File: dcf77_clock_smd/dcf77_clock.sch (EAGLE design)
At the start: 24 parts, among them IC1 7805DT, IC2 ATMEGA48/88/168-AU, J2 DCJ0202, U1 LCD-16X2SILK

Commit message: Update capacitors footprints
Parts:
- removed EN1: PEC11, bourns:PEC11
- added C3: (no value), rcl:CPOL-EUSMCZ
- added SW1: EC12E_SW, switch-alps:EC12E_SW
- C2: device rcl:CPOL-EUE2-5 -> rcl:CPOL-EUUD-4X5,8
- LED1: device SparkFun:LED-FKIT-1206 -> led:LEDCHIP-LED0805
- Q1: device crystal:CRYSTALSM49 -> crystal:CRYSTALMM39SL
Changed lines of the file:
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@@
 <part name="U$1" library="SparkFun" deviceset="AVR_SPI_PROG2" device="PTH2"/>
 <part name="U1" library="SparkFun" deviceset="LCD-16X2" device="SILK"/>
-<part name="LED1" library="SparkFun" deviceset="LED" device="-FKIT-1206"/>
+<part name="LED1" library="led" library_urn="urn:adsk.eagle:library:259" deviceset="LED" device="CHIP-LED0805" package3d_urn="urn:adsk.eagle:package:15818/2"/>
 <part name="IC2" library="atmega8" deviceset="ATMEGA48/88/168" device="-AU"/>
 <part name="U$4" library="SparkFun" deviceset="DS1307" device="SO8"/>
 <part name="IC1" library="linear" library_urn="urn:adsk.eagle:library:262" deviceset="78*" device="DT" package3d_urn="urn:adsk.eagle:package:16415/2" technology="05" value="7805DT"/>
 <part name="J2" library="con-jack" library_urn="urn:adsk.eagle:library:154" deviceset="DCJ0202" device="" package3d_urn="urn:adsk.eagle:package:7491/1"/>
-<part name="Q1" library="crystal" library_urn="urn:adsk.eagle:library:204" deviceset="CRYSTAL" device="SM49" package3d_urn="urn:adsk.eagle:package:12085/1"/>
+<part name="Q1" library="crystal" library_urn="urn:adsk.eagle:library:204" deviceset="CRYSTAL" device="MM39SL" package3d_urn="urn:adsk.eagle:package:12090/1"/>
 <part name="R1" library="SparkFun" deviceset="TRIMPOT" device="PTH"/>
 <part name="H1" library="holes" library_urn="urn:adsk.eagle:library:237" deviceset="MOUNT-HOLE" device="3.2" package3d_urn="urn:adsk.eagle:package:14275/1" value="MOUNT-HOLE3.2"/>
@@
 <part name="GND1" library="supply1" library_urn="urn:adsk.eagle:library:371" deviceset="GND" device=""/>
 <part name="C1" library="rcl" library_urn="urn:adsk.eagle:library:334" deviceset="C-EU" device="C0805K" package3d_urn="urn:adsk.eagle:package:23681/2" value="100n"/>
-<part name="EN1" library="bourns" deviceset="PEC11" device=""/>
 <part name="L1" library="rcl" library_urn="urn:adsk.eagle:library:334" deviceset="L-EU" device="L1812" package3d_urn="urn:adsk.eagle:package:23494/2"/>
-<part name="C2" library="rcl" library_urn="urn:adsk.eagle:library:334" deviceset="CPOL-EU" device="E2-5" package3d_urn="urn:adsk.eagle:package:23346/2"/>
+<part name="C2" library="rcl" library_urn="urn:adsk.eagle:library:334" deviceset="CPOL-EU" device="UD-4X5,8" package3d_urn="urn:adsk.eagle:package:23474/1"/>
 <part name="MOD1" library="dcf77" deviceset="DCF77MODULE" device=""/>
 <part name="HOLD1" library="dcf77" deviceset="COREHOLDER" device=""/>
@@
 <part name="H3" library="holes" library_urn="urn:adsk.eagle:library:237" deviceset="MOUNT-HOLE" device="3.2" package3d_urn="urn:adsk.eagle:package:14275/1" value="MOUNT-HOLE3.2"/>
 <part name="H4" library="holes" library_urn="urn:adsk.eagle:library:237" deviceset="MOUNT-HOLE" device="3.2" package3d_urn="urn:adsk.eagle:package:14275/1" value="MOUNT-HOLE3.2"/>
+<part name="SW1" library="switch-alps" library_urn="urn:adsk.eagle:library:373" deviceset="EC12E_SW" device="" package3d_urn="urn:adsk.eagle:package:27083/1"/>
+<part name="C3" library="rcl" library_urn="urn:adsk.eagle:library:334" deviceset="CPOL-EU" device="SMCZ" package3d_urn="urn:adsk.eagle:package:25927/3"/>
 </parts>
 <sheets>
@@
 <attribute name="VALUE" x="-9.144" y="13.081" size="1.778" layer="96" rot="MR0"/>
 </instance>
-<instance part="EN1" gate="1" x="99.06" y="30.48" smashed="yes">
-<attribute name="NAME" x="95.25" y="35.56" size="1.778" layer="95"/>
-<attribute name="VALUE" x="93.98" y="24.13" size="1.778" layer="96"/>
-</instance>
 <instance part="L1" gate="G$1" x="-45.72" y="86.36" smashed="yes">
 <attribute name="NAME" x="-54.8386" y="143.51" size="1.778" layer="95" rot="R90"/>
@@
 <attribute name="VALUE" x="144.272" y="-35.4838" size="1.778" layer="96"/>
 </instance>
+<instance part="SW1" gate="G$1" x="129.54" y="106.68" smashed="yes">
+<attribute name="PART" x="125.73" y="106.68" size="1.27" layer="95" rot="R90"/>
+<attribute name="VALUE" x="135.89" y="106.68" size="1.27" layer="96" rot="R90"/>
+</instance>
+<instance part="SW1" gate="G$2" x="149.86" y="114.3" smashed="yes">
+<attribute name="PART" x="144.78" y="119.38" size="1.27" layer="95"/>
+<attribute name="VALUE" x="144.78" y="111.76" size="1.27" layer="96"/>
+</instance>
+<instance part="C3" gate="G$1" x="-127" y="83.82" smashed="yes">
+<attribute name="NAME" x="-125.857" y="84.3026" size="1.778" layer="95"/>
+<attribute name="VALUE" x="-125.857" y="79.2226" size="1.778" layer="96"/>
+</instance>
 </instances>

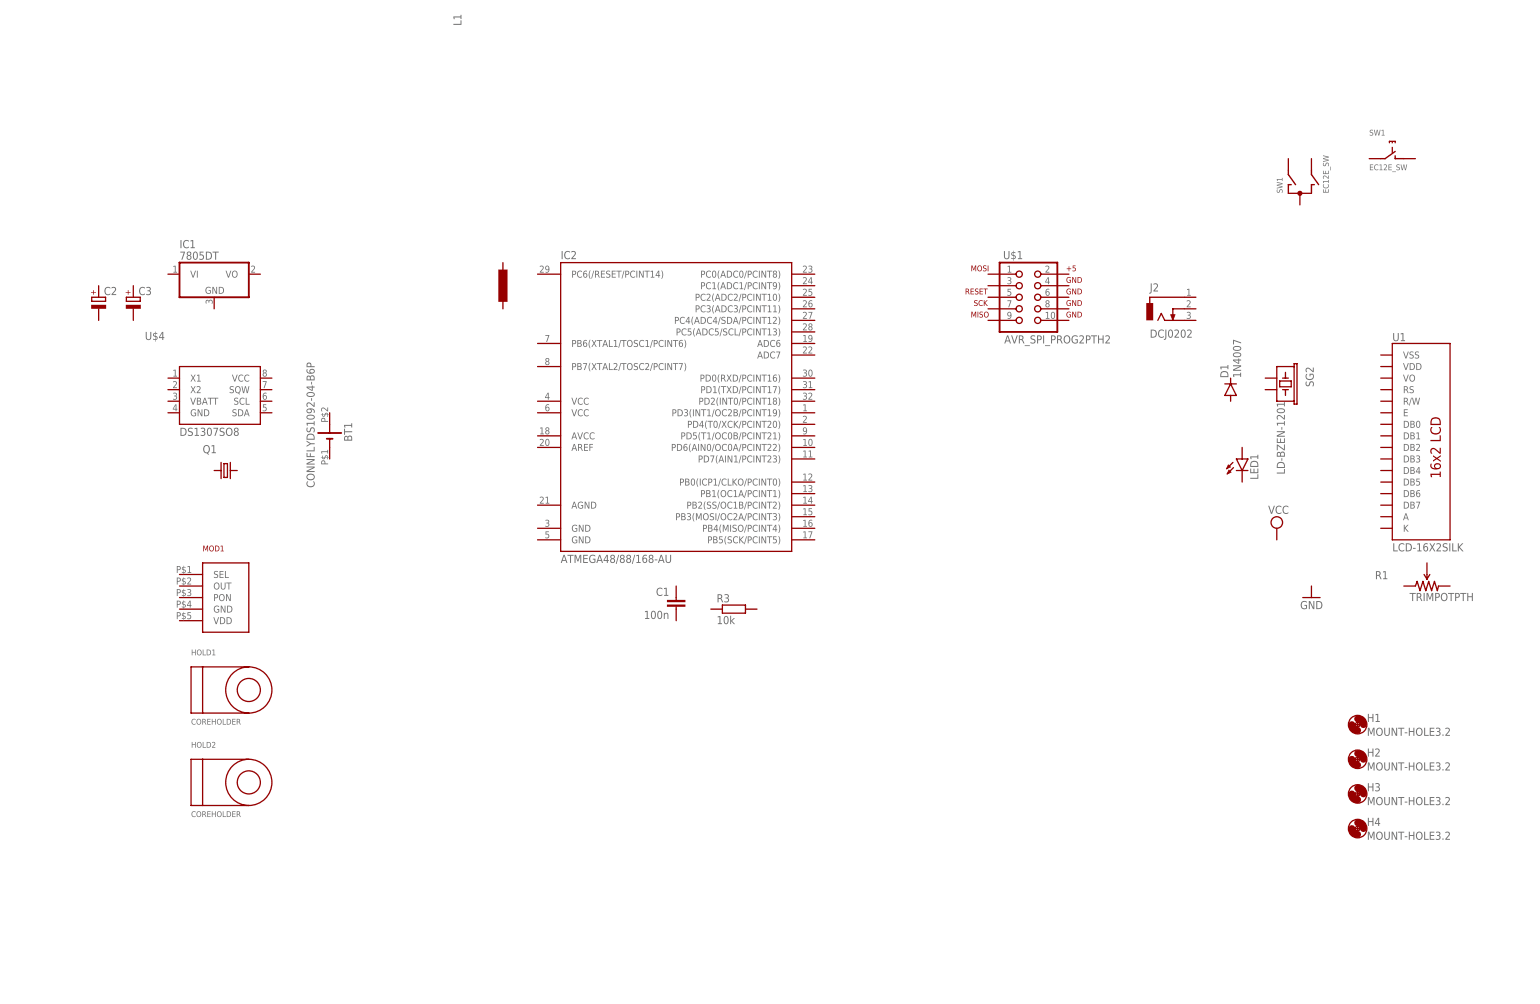
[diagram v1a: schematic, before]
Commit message: Add power supply and basic components schematic
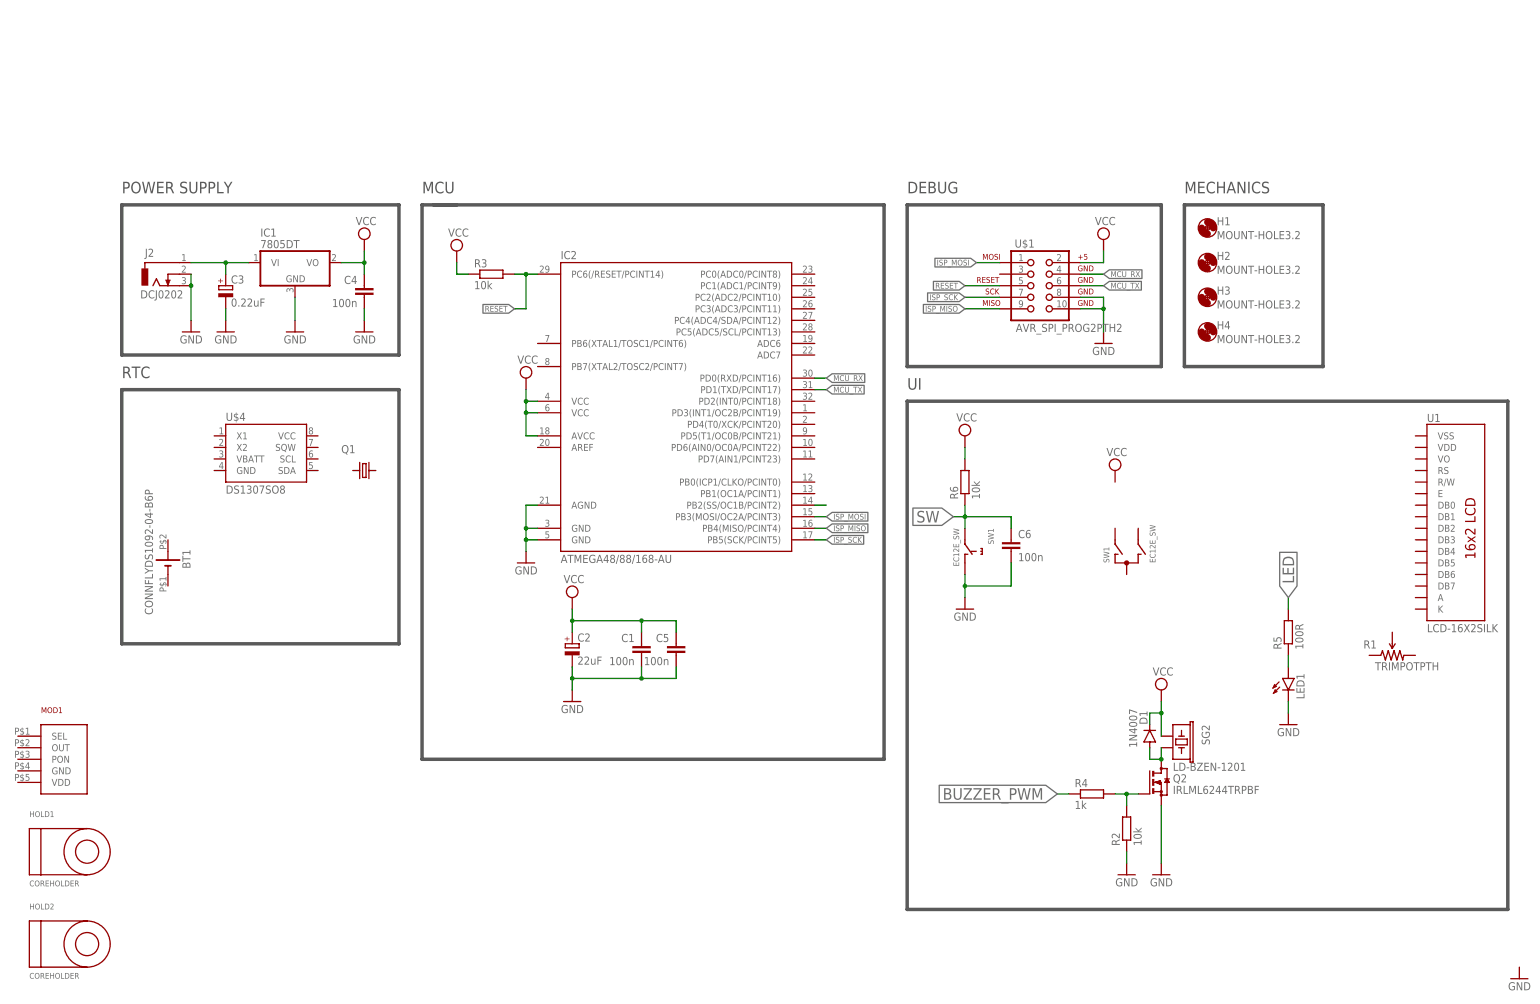
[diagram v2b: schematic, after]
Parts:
- removed L1: (no value), rcl:L-EUL1812
- added C4, C5, C6: 100n, rcl:C-EUC0805K
- added Q2: IRLML6244TRPBF, sosbutton:IRLML6244TRPBF
- added R2, R6: 10k, rcl:R-EU_M0805
- added R4: 1k, rcl:R-EU_M0805
- added R5: 100R, rcl:R-EU_M0805
- C2: value (none) -> 22uF
- C3: value (none) -> 0.22uF
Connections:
- new net BUZZER_PWM: R4.1
- new net GND: C1.2, C2.-, C3.-, C4.2, C5.2, C6.2, IC1.GND, IC2.AGND, IC2.GND@1, IC2.GND@2, J2.2, J2.3, LED1.C, Q2.S, R2.1, SW1G$2.1, U$1.10, U$1.8
- new net ISP_MISO: IC2.PB4(MISO/PCINT4), U$1.9
- new net ISP_MOSI: IC2.PB3(MOSI/OC2A/PCINT3), U$1.1
- new net ISP_SCK: IC2.PB5(SCK/PCINT5), U$1.7
- new net LED: R5.2
- new net MCU_RX: IC2.PD0(RXD/PCINT16), U$1.4
- new net MCU_TX: IC2.PD1(TXD/PCINT17), U$1.6
- new net N$1: C3.+, IC1.VI, J2.1
- new net N$2: D1.A, Q2.D, SG2.2
- new net N$3: Q2.G, R2.2, R4.2
- new net N$4: LED1.A, R5.1
- new net N$8: IC2.PB2(SS/OC1B/PCINT2)
- new net RESET: IC2.PC6(/RESET/PCINT14), R3.2, U$1.5
- new net SW: C6.1, R6.1, SW1G$2.2
- new net VCC: C1.1, C2.+, C4.1, C5.1, D1.C, IC1.VO, IC2.AVCC, IC2.VCC@1, IC2.VCC@2, R3.1, R6.2, SG2.1, U$1.2
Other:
- note added: "DEBUG"
- note added: "MCU"
- note added: "MECHANICS"
- note added: "POWER SUPPLY"
- note added: "RTC"
- note added: "UI"
- moved on the sheet: BT1, C1, C2, C3, D1, H1, H2, H3, H4, HOLD1, HOLD2, IC1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

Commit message: Add first complete version of schematic
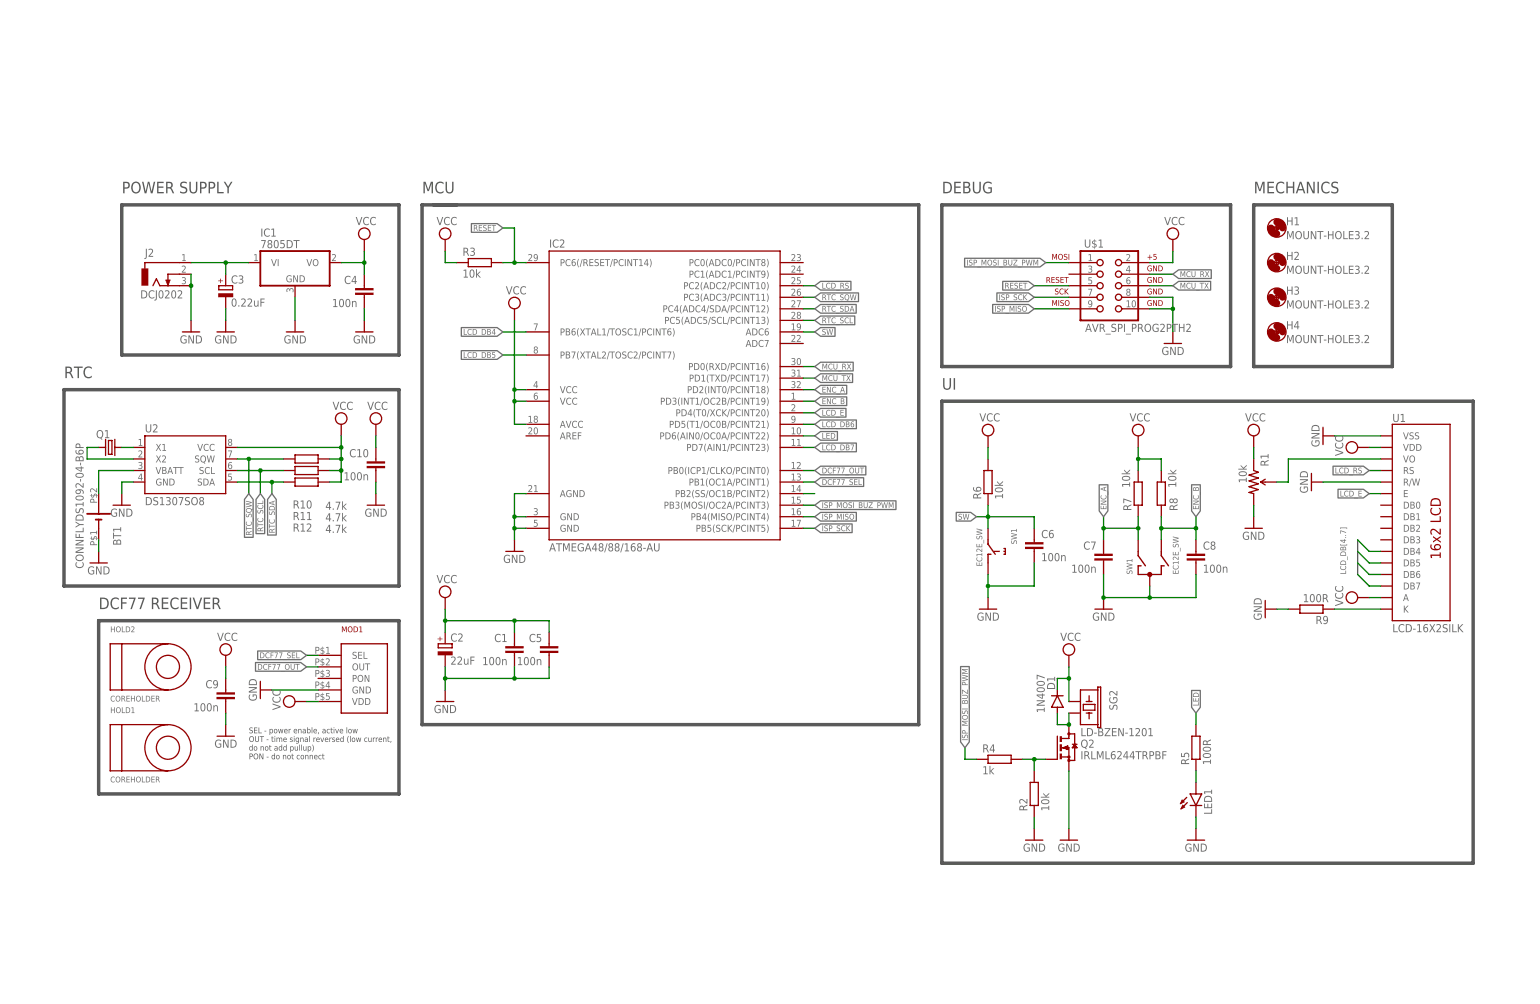
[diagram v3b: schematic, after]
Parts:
- removed U$4: DS1307SO8, SparkFun:DS1307SO8
- added C10, C7, C8, C9: 100n, rcl:C-EUC0805K
- added R10, R11, R12: 4.7k, rcl:R-EU_M0805
- added R7, R8: 10k, rcl:R-EU_M0805
- added R9: 100R, rcl:R-EU_M0805
- added U2: DS1307SO8, SparkFun:DS1307SO8
- R1: value TRIMPOTPTH -> 10k
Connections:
- removed net BUZZER_PWM: R4.1
- removed net ISP_MOSI: IC2.PB3(MOSI/OC2A/PCINT3), U$1.1
- new net DCF77_OUT: IC2.PB0(ICP1/CLKO/PCINT0), MOD1.OUT
- new net DCF77_SEL: IC2.PB1(OC1A/PCINT1), MOD1.SEL
- new net ENC_A: C7.1, IC2.PD2(INT0/PCINT18), R7.1, SW1G$1.A
- new net ENC_B: C8.1, IC2.PD3(INT1/OC2B/PCINT19), R8.1, SW1G$1.B
- new net ISP_MOSI_BUZ_PWM: IC2.PB3(MOSI/OC2A/PCINT3), R4.1, U$1.1
- new net LCD_DB4: IC2.PB6(XTAL1/TOSC1/PCINT6), U1.DB4
- new net LCD_DB5: IC2.PB7(XTAL2/TOSC2/PCINT7), U1.DB5
- new net LCD_DB6: IC2.PD5(T1/OC0B/PCINT21), U1.DB6
- new net LCD_DB7: IC2.PD7(AIN1/PCINT23), U1.DB7
- new net LCD_E: IC2.PD4(T0/XCK/PCINT20), U1.E
- new net LCD_RS: IC2.PC2(ADC2/PCINT10), U1.RS
- new net N$10: Q1.1, U2.X1
- new net N$11: Q1.2, U2.X2
- new net N$12: BT1.+, U2.VBATT
- new net N$7: R1.WIPER, U1.VO
- new net N$9: R9.1, U1.K
- new net RTC_SCL: IC2.PC5(ADC5/SCL/PCINT13), R11.2, U2.SCL
- new net RTC_SDA: IC2.PC4(ADC4/SDA/PCINT12), R12.2, U2.SDA
- new net RTC_SQW: IC2.PC3(ADC3/PCINT11), R10.2, U2.SQW
- net GND: now also BT1.-, C10.2, C7.2, C8.2, C9.2, MOD1.GND, R1.CW, R9.2, SW1G$1.C, U1.R/W, U1.VSS, U2.GND
- net LED: now also IC2.PD6(AIN0/OC0A/PCINT22)
- net SW: now also IC2.ADC6
- net VCC: now also C10.1, C9.1, MOD1.VDD, R1.CCW, R10.1, R11.1, R12.1, R7.2, R8.2, U1.A, U1.VDD, U2.VCC
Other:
- note added: "DCF77 RECEIVER"
- note added: "SEL - power enable, active low OUT - time signal reversed (low current, do not add pullup) PON - do not connect"
- moved on the sheet: BT1, C1, C2, C5, C6, D1, H1, H2, H3, H4, HOLD1, HOLD2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
